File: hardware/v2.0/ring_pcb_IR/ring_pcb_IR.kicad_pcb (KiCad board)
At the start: 2 copper layers, 19.1 x 19.1 mm, 22 parts, among them Q1 Q_PNP_BEC, Q2 Q_Dual_NPN_NPN_C2E2C1E1B1B2, Q3 Q_Dual_NPN_NPN_C2E2C1E1B1B2, U2 ATtiny85-20M

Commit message: Add collector connection for PNP
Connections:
- Q1 pad 3: unconnected-(Q1-C-Pad3) -> GND

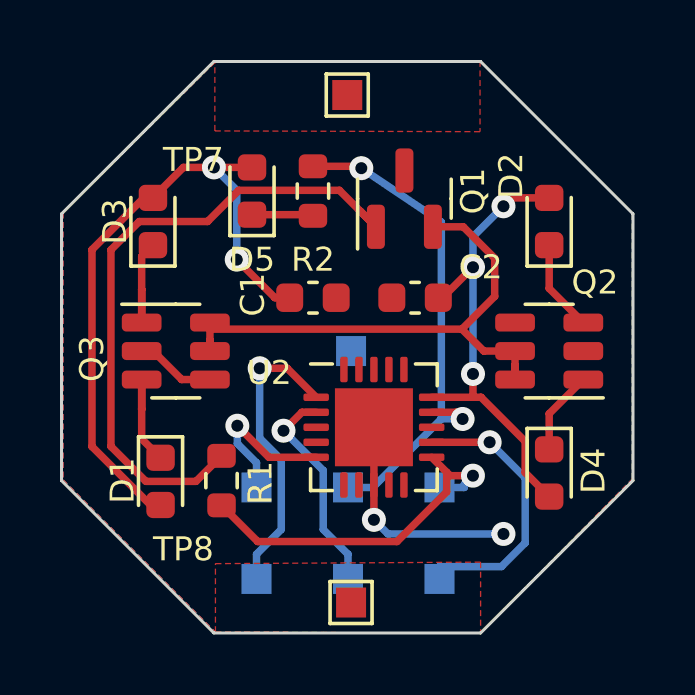
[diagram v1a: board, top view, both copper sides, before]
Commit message: Routed with smaller PCB
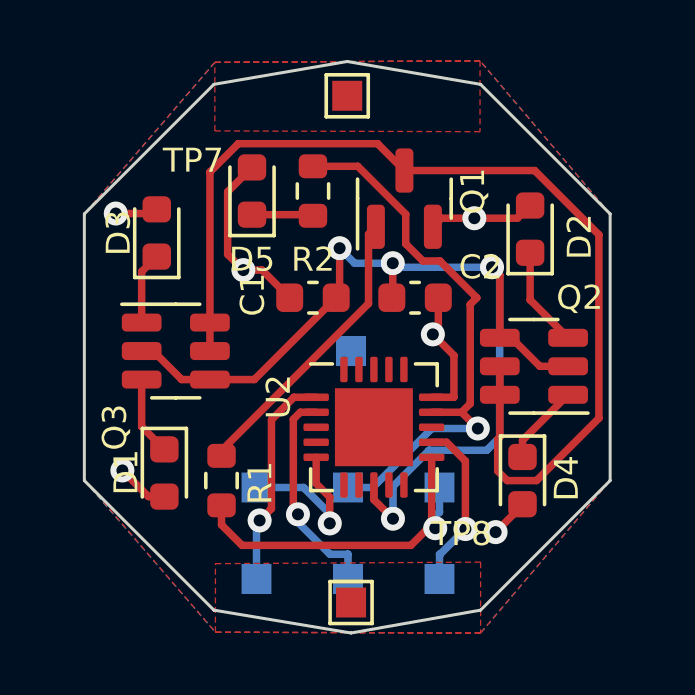
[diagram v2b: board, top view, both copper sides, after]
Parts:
- moved D4 0.92 mm to (142.4, 115.6)
- moved Q2 0.72 mm to (142.7, 111.8)
- moved D2 0.68 mm to (142.6, 107.2)
- moved D3 0.40 mm to (130.2, 107.3)
- moved D1 0.31 mm to (130.4, 115.3)
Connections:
- Q1 pad 2: Net-(Q1-E) -> VCC
- Q1 pad 3: GND -> Net-(Q1-C)
- Q2 pad 5: Net-(Q1-E) -> Net-(Q1-C)
- Q2 pad 6: Net-(Q1-E) -> Net-(Q1-C)
- Q3 pad 5: Net-(Q1-E) -> Net-(Q1-C)
- Q3 pad 6: Net-(Q1-E) -> Net-(Q1-C)
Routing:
- net Net-(Q1-C): track 0.00 -> 34.6 mm
- net GND: track 10.3 -> 33.8 mm, vias 2 -> 4
- net VCC: track 37.7 -> 18.3 mm, vias 5 -> 6
- net Net-(Q1-E): track 19.1 -> 0.00 mm
- net Net-(Q1-B): track 22.0 -> 9.77 mm
- net PB1: track 9.79 -> 5.69 mm
- net PB5: track 10.4 -> 7.31 mm
- net Net-(D3-K): track 4.10 -> 2.41 mm
- net PB2: track 17.3 -> 18.8 mm, vias 2 -> 1
- net Net-(D1-K): track 3.86 -> 2.64 mm
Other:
- board size 19.1 x 19.1 mm -> 17.5 x 19.1 mm

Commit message: Change transistors and rewire
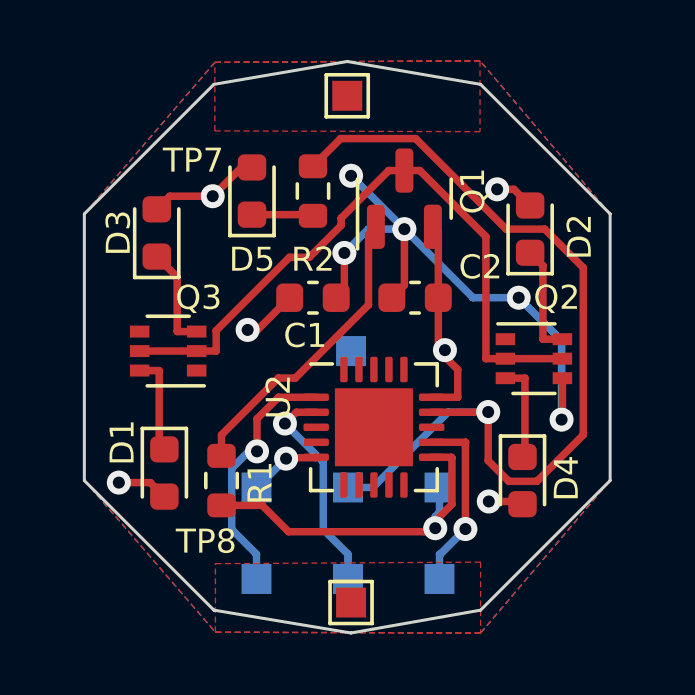
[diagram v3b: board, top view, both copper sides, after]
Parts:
- Q2, Q3: value Q_Dual_NPN_NPN_C2E2C1E1B1B2 -> Q_Dual_NPN_NPN_E1B1C2E2B2C1; footprint Package_TO_SOT_SMD:SOT-23-6 -> Package_TO_SOT_SMD:SOT-363_SC-70-6
- moved Q2 0.25 mm to (142.7, 111.5), turned to 0 degrees
- moved Q3 0.25 mm to (130.6, 111.3), turned to 180 degrees
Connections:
- Q2 pad 1: Net-(D4-K) -> GND
- Q2 pad 2: GND -> Net-(Q1-C)
- Q2 pad 3: Net-(D2-K) -> Net-(D4-K)
- Q2 pad 6: Net-(Q1-C) -> Net-(D2-K)
- Q3 pad 1: Net-(D3-K) -> GND
- Q3 pad 2: GND -> Net-(Q1-C)
- Q3 pad 3: Net-(D1-K) -> Net-(D3-K)
- Q3 pad 6: Net-(Q1-C) -> Net-(D1-K)
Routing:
- net GND: track 33.8 -> 19.7 mm, vias 4 -> 5
- net Net-(Q1-C): track 34.6 -> 22.1 mm
- net PB2: track 18.8 -> 30.1 mm
- net PB4: track 5.52 -> 2.41 mm
- net VCC: track 18.3 -> 16.9 mm
- net PB5: track 7.31 -> 8.46 mm
- net Net-(D3-K): track 2.41 -> 3.43 mm
- net Net-(D1-K): track 2.64 -> 3.35 mm
- net Net-(D4-K): track 2.70 -> 3.31 mm

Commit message: New Gerbers with smaller dual-NPN
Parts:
- C2: value 100u -> 10u
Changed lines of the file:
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@@
     (descr "Resistor SMD 0603 (1608 Metric), square (rectangular) end terminal, IPC_7351 nominal, (Body size source: IPC-SM-782 page 72, https://www.pcb-3d.com/wordpress/wp-content/uploads/ipc-sm-782a_amendment_1_and_2.pdf), generated with kicad-footprint-generator")
     (tags "resistor")
-    (property "MPN" "")
+    (property "MPN" "RT0603FRE101KL")
     (property "Sheetfile" "ring_pcb_IR.kicad_sch")
     (property "Sheetname" "")
@@
     (descr "SOT, 3 Pin (https://www.jedec.org/system/files/docs/to-236h.pdf variant AB), generated with kicad-footprint-generator ipc_gullwing_generator.py")
     (tags "SOT TO_SOT_SMD")
-    (property "MPN" "")
+    (property "MPN" "MMBTA55LT1G")
     (property "Sheetfile" "ring_pcb_IR.kicad_sch")
     (property "Sheetname" "")
@@
     (descr "SMD rectangular pad as test Point, square 1.0mm side length")
     (tags "test point SMD pad rectangle square")
-    (property "MPN" "")
+    (property "MPN" "DNP")
     (property "Sheetfile" "ring_pcb_IR.kicad_sch")
     (property "Sheetname" "")
@@
     (descr "SOT-363, SC-70-6")
     (tags "SOT-363 SC-70-6")
+    (property "MPN" "BC847BS,115")
     (property "Sheetfile" "ring_pcb_IR.kicad_sch")
     (property "Sheetname" "")
@@
     (descr "SMD rectangular pad as test Point, square 1.0mm side length")
     (tags "test point SMD pad rectangle square")
-    (property "MPN" "")
+    (property "MPN" "DNP")
     (property "Sheetfile" "ring_pcb_IR.kicad_sch")
     (property "Sheetname" "")
@@
     (descr "SOT-363, SC-70-6")
     (tags "SOT-363 SC-70-6")
+    (property "MPN" "BC847BS,115")
     (property "Sheetfile" "ring_pcb_IR.kicad_sch")
     (property "Sheetname" "")
@@
     (descr "QFN, 20 Pin (http://ww1.microchip.com/downloads/en/DeviceDoc/doc2535.pdf#page=164), generated with kicad-footprint-generator ipc_noLead_generator.py")
     (tags "QFN NoLead")
-    (property "MPN" "")
+    (property "MPN" "ATTINY85-20MU")
     (property "Sheetfile" "ring_pcb_IR.kicad_sch")
     (property "Sheetname" "")
@@
     (fp_line (start 2 2) (end -2 2)
       (stroke (width 0.1) (type solid)) (layer "F.Fab"))
-    (pad "" smd roundrect (at -0.65 -0.65) (size 1.05 1.05) (layers "F.Paste") (roundrect_rratio 0.2380952381))
-    (pad "" smd roundrect (at -0.65 0.65) (size 1.05 1.05) (layers "F.Paste") (roundrect_rratio 0.2380952381))
-    (pad "" smd roundrect (at 0.65 -0.65) (size 1.05 1.05) (layers "F.Paste") (roundrect_rratio 0.2380952381))
-    (pad "" smd roundrect (at 0.65 0.65) (size 1.05 1.05) (layers "F.Paste") (roundrect_rratio 0.2380952381))
+    (pad "" smd roundrect (at -0.65 -0.65) (size 1.05 1.05) (layers "F.Paste") (roundrect_rratio 0.238095))
+    (pad "" smd roundrect (at -0.65 0.65) (size 1.05 1.05) (layers "F.Paste") (roundrect_rratio 0.238095))
+    (pad "" smd roundrect (at 0.65 -0.65) (size 1.05 1.05) (layers "F.Paste") (roundrect_rratio 0.238095))
+    (pad "" smd roundrect (at 0.65 0.65) (size 1.05 1.05) (layers "F.Paste") (roundrect_rratio 0.238095))
     (pad "1" smd roundrect (at -1.925 -1) (size 0.85 0.25) (layers "F.Cu" "F.Paste" "F.Mask") (roundrect_rratio 0.25)
       (net 27 "PB5") (pinfunction "~{RESET}/PB5") (pintype "bidirectional"))
@@
       (rotate (xyz 0 0 0))
     )
-    (model ":KICAD7_3DMODEL_DIR:Package_DFN_QFN.3dshapes/QFN-20-1EP_4x4mm_P0.5mm.step"
-      (offset (xyz 0 0 0))
-      (scale (xyz 1 1 1))
-      (rotate (xyz 0 0 0))
-    )
   )
   (footprint "Capacitor_SMD:C_0603_1608Metric" (layer "F.Cu")
@@
     (descr "Capacitor SMD 0603 (1608 Metric), square (rectangular) end terminal, IPC_7351 nominal, (Body size source: IPC-SM-782 page 76, https://www.pcb-3d.com/wordpress/wp-content/uploads/ipc-sm-782a_amendment_1_and_2.pdf), generated with kicad-footprint-generator")
     (tags "capacitor")
-    (property "MPN" "")
+    (property "MPN" "GRM188R61A106KE69J")
     (property "Sheetfile" "ring_pcb_IR.kicad_sch")
     (property "Sheetname" "")
@@
         (effects (font (size 0.8 0.8) (thickness 0.2)))
     )
-    (fp_text value "100u" (at 0 1.43) (layer "F.Fab")
+    (fp_text value "10u" (at 0 1.43) (layer "F.Fab")
         (effects (font (size 1 1) (thickness 0.15)))
     )
@@
     (descr "Resistor SMD 0603 (1608 Metric), square (rectangular) end terminal, IPC_7351 nominal, (Body size source: IPC-SM-782 page 72, https://www.pcb-3d.com/wordpress/wp-content/uploads/ipc-sm-782a_amendment_1_and_2.pdf), generated with kicad-footprint-generator")
     (tags "resistor")
-    (property "MPN" "")
+    (property "MPN" "RT0603BRD07210RL")
     (property "Sheetfile" "ring_pcb_IR.kicad_sch")
     (property "Sheetname" "")
@@
     (descr "SMD rectangular pad as test Point, square 1.0mm side length")
     (tags "test point SMD pad rectangle square")
-    (property "MPN" "")
+    (property "MPN" "DNP")
     (property "Sheetfile" "ring_pcb_IR.kicad_sch")
     (property "Sheetname" "")
@@
     (descr "SMD rectangular pad as test Point, square 1.0mm side length")
     (tags "test point SMD pad rectangle square")
-    (property "MPN" "")
+    (property "MPN" "DNP")
     (property "Sheetfile" "ring_pcb_IR.kicad_sch")
     (property "Sheetname" "")
@@
     (descr "SMD rectangular pad as test Point, square 1.0mm side length")
     (tags "test point SMD pad rectangle square")
-    (property "MPN" "")
+    (property "MPN" "DNP")
     (property "Sheetfile" "ring_pcb_IR.kicad_sch")
     (property "Sheetname" "")
@@
     (descr "SMD rectangular pad as test Point, square 1.0mm side length")
     (tags "test point SMD pad rectangle square")
-    (property "MPN" "")
+    (property "MPN" "DNP")
     (property "Sheetfile" "ring_pcb_IR.kicad_sch")
     (property "Sheetname" "")
@@
     (descr "SMD rectangular pad as test Point, square 1.0mm side length")
     (tags "test point SMD pad rectangle square")
-    (property "MPN" "")
+    (property "MPN" "DNP")
     (property "Sheetfile" "ring_pcb_IR.kicad_sch")
     (property "Sheetname" "")
@@
     (descr "SMD rectangular pad as test Point, square 1.0mm side length")
     (tags "test point SMD pad rectangle square")
-    (property "MPN" "")
+    (property "MPN" "DNP")
     (property "Sheetfile" "ring_pcb_IR.kicad_sch")
     (property "Sheetname" "")
@@
     (descr "SMD rectangular pad as test Point, square 1.0mm side length")
     (tags "test point SMD pad rectangle square")
-    (property "MPN" "")
-    (property "Sheetfile" "ring_pcb_IR.kicad_sch")
-    (property "Sheetname" "")
+    (property "MPN" "DNP")
+    (property "Sheetfile" "ring_pcb_IR.kicad_sch")
+    (property "Sheetname" "")
